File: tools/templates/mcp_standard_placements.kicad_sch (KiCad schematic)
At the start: 150 parts, among them J1 ICSP, J3 PIR BOARD, J5 MOTOR, J6 DNP, Q1 FMOS3401A?, Q11 MMBTA55?, Q2 BC847B?, Q3 MMBTA55?, Q4 MMBTA55?, Q5 MMBTA55?, Q6 MMBTA55?, Q7 BC857C?, Q8 N/P pair? (372A), Q9 DNP, U1 S-1200B45? [pins], U106 U6A / DNP, U2 SN74LVC2G14DBV?, U3 SGM8542XS, U4 PIC16F18855, U5 MX512H, U6 S-812C33AMC? / 3.3V, U7 DNP, Y1 20 MHz

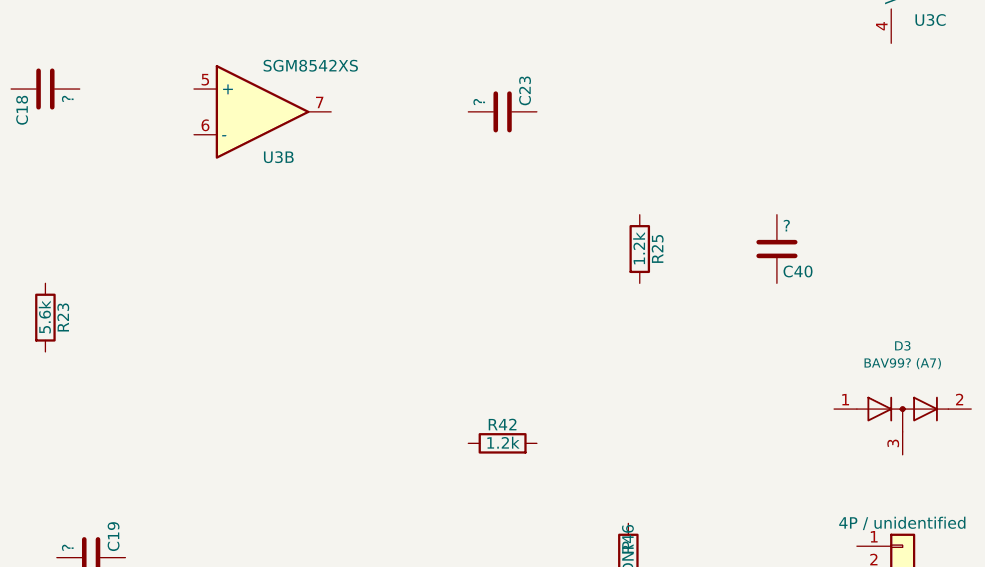
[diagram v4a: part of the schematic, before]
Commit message: Resolve R23 junction and require photo tracing before bench requests
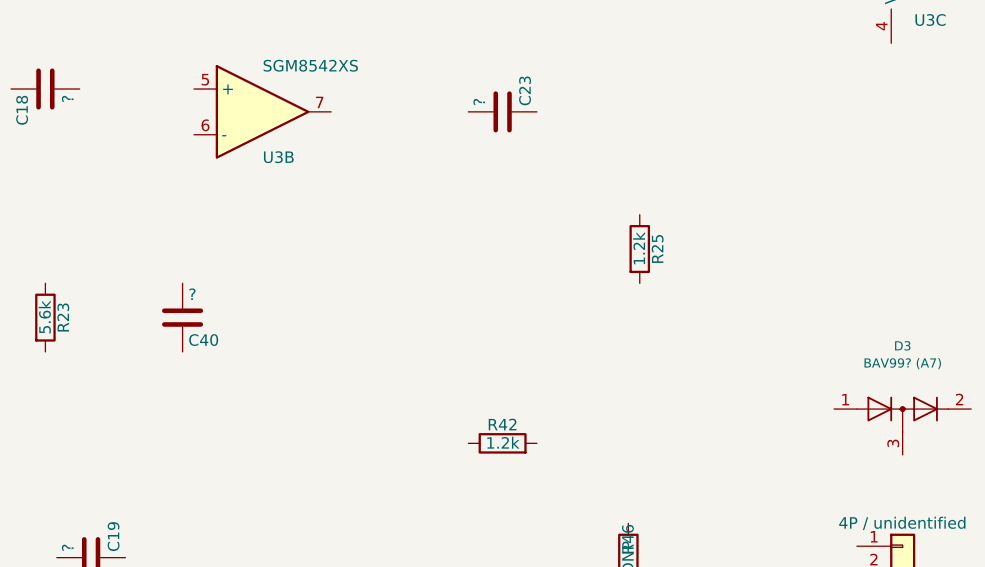
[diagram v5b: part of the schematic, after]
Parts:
- C40: MeasurementEvidence (none) -> v0.9.15: lower P/model1 joins R23 C/model2 and R42 Q/model1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; ViaEvidence v0.9.2: V083 associated with C40; earlier GND report retain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 -> v0.9.15: lower P/model1 joins R23 C/model2 and R42 Q/model1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
- R23: MeasurementEvidence v0.9.14 user: B/left/model1-U3.6 1 ohm; C/right/model2-U3.6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 -> v0.9.15: right C/model2 joins C40 lower P/model1 and R42 up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; ViaEvidence v0.9.14 user: B/left/model1-U3.6 1 ohm; C/right/model2-U3.6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 -> v0.9.15: right C/model2 joins C40 lower P/model1 and R42 up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
- R42: MeasurementEvidence (none) -> v0.9.15: upper Q/model1 joins R23 C/model2 and C40 P/model1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; ViaEvidence v0.9.8: User confirms V017-TP4. Prior V017-R42.1/R44.1 loca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 -> v0.9.15: upper Q/model1 joins R23 C/model2 and C40 P/model1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
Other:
- moved on the sheet: C40
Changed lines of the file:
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@@
 			)
 		)
-    (property "MeasurementEvidence" "v0.9.14 user: pin5-VREF/R22 D 1 ohm (batch1); pin6-R23 B/left/model1 1 ohm and C/right/model2 5.6 kohm. Pin6-R22 E/GND 400 kohm. Pin5 and pin6 remain distinct; C18 branch is retained photo evidence, not meter-confirmed." (at 381.0 200.66 0)
-      (effects (font (size 1.27 1.27)) (hide yes))
-    )
+		(property "MeasurementEvidence" "v0.9.14 user: pin5-VREF/R22 D 1 ohm (batch1); pin6-R23 B/left/model1 1 ohm and C/right/model2 5.6 kohm. Pin6-R22 E/GND 400 kohm. Pin5 and pin6 remain distinct; C18 branch is retained photo evidence, not meter-confirmed."
+			(at 381.0 200.66 0)
+			(effects
+				(font
+					(size 1.27 1.27)
+				)
+				(hide yes)
+			)
+		)
 		(pin "1"
 		)
@@
 			)
 		)
-		(property "ViaEvidence" "v0.9.14 user: B/left/model1-U3.6 1 ohm; C/right/model2-U3.6 5.6 kohm, agreeing with 562 marking. C destination remains open; earlier VREF guess rejected by 270-289 kohm to pin5. Pin6-GND 400 kohm also rejects a direct pin6-ground join."
+		(property "ViaEvidence" "v0.9.15: right C/model2 joins C40 lower P/model1 and R42 upper Q/model1 at 1 ohm each. Left B/model1 joins U3.6 (prior 1 ohm); marked 5.6k retained. C18 ends/TP6/VREF direct joins rejected by prior high readings. R42.1 remote PIC/TP4 association retained from earlier user reports."
+			(at 461.01 223.52 0)
+			(effects
+				(font
+					(size 1.27 1.27)
+				)
+				(hide yes)
+			)
+		)
+		(property "MeasurementEvidence" "v0.9.15: right C/model2 joins C40 lower P/model1 and R42 upper Q/model1 at 1 ohm each. Left B/model1 joins U3.6 (prior 1 ohm); marked 5.6k retained. C18 ends/TP6/VREF direct joins rejected by prior high readings. R42.1 remote PIC/TP4 association retained from earlier user reports."
 			(at 461.01 223.52 0)
 			(effects
 				(font
 					(size 1.27 1.27)
-				) (hide yes))
+				)
+				(hide yes)
+			)
 		)
-    (property "MeasurementEvidence" "v0.9.14 user: B/left/model1-U3.6 1 ohm; C/right/model2-U3.6 5.6 kohm, agreeing with 562 marking. C destination remains open; earlier VREF guess rejected by 270-289 kohm to pin5. Pin6-GND 400 kohm also rejects a direct pin6-ground join." (at 461.01 223.52 0)
-      (effects (font (size 1.27 1.27)) (hide yes))
-    )
 		(pin "1"
 		)
@@
 	(symbol
 		(lib_id "Device:C")
-		(at 542.29 215.9 0)
+		(at 476.25 223.52 0)
 		(unit 1)
 		(body_style 1)
@@
 		(dnp no)
 		(property "Reference" "C40"
-			(at 542.925 218.44 0)
+			(at 476.885 226.06 0)
 			(show_name no)
 			(do_not_autoplace no)
@@
 		)
 		(property "Value" "?"
-			(at 542.925 213.36 0)
+			(at 476.885 220.98000000000002 0)
 			(show_name no)
 			(do_not_autoplace no)
@@
 		)
 		(property "Footprint" "Capacitor_SMD:C_0805_2012Metric"
-			(at 543.255 212.09 0)
+			(at 477.21500000000003 219.71 0)
 			(hide yes)
 			(show_name no)
@@
 		)
 		(property "Datasheet" ""
-			(at 542.29 215.9 0)
+			(at 476.25 223.52 0)
 			(hide yes)
 			(show_name no)
@@
 		)
 		(property "Description" "Unpolarized capacitor"
-			(at 542.29 215.9 0)
+			(at 476.25 223.52 0)
 			(hide yes)
 			(show_name no)
@@
 			)
 		)
-		(property "ViaEvidence" "v0.9.2: V083 associated with C40; earlier GND report retained for photo-selected return pad2."
-			(at 542.29 215.9 0)
+		(property "ViaEvidence" "v0.9.15: lower P/model1 joins R23 C/model2 and R42 Q/model1, user 1 ohm. Remove prior C23/R25 detector-output association. Upper/model2 remains GND via user V083 report plus photo pad selection. Capacitance unmeasured."
+			(at 476.25 223.52 0)
+			(effects
+				(font
+					(size 1.27 1.27)
+				)
+				(hide yes)
+			)
+		)
+		(property "MeasurementEvidence" "v0.9.15: lower P/model1 joins R23 C/model2 and R42 Q/model1, user 1 ohm. Remove prior C23/R25 detector-output association. Upper/model2 remains GND via user V083 report plus photo pad selection. Capacitance unmeasured."
+			(at 476.25 223.52 0)
 			(effects
 				(font
@@
 			)
 		)
-		(property "ViaEvidence" "v0.9.8: User confirms V017-TP4. Prior V017-R42.1/R44.1 local junction now joins TP4 and PIC25/RB4. R42.1 explicitly user-named; R44 pad1 and C41 branch retain earlier photo selection. No numeric resistance supplied; circuit operating role remains inferred."
+		(property "ViaEvidence" "v0.9.15: upper Q/model1 joins R23 C/model2 and C40 P/model1 at 1 ohm. Prior V017/TP4/PIC25/R44.1 mapping retained. Lower/model2 to D3.S is photo-selected, supported by earlier component-level 1.2 ohm reading without named end. Marked 1.2k retained."
+			(at 511.81 237.49 0)
+			(effects
+				(font
+					(size 1.27 1.27)
+				)
+				(hide yes)
+			)
+		)
+		(property "MeasurementEvidence" "v0.9.15: upper Q/model1 joins R23 C/model2 and C40 P/model1 at 1 ohm. Prior V017/TP4/PIC25/R44.1 mapping retained. Lower/model2 to D3.S is photo-selected, supported by earlier component-level 1.2 ohm reading without named end. Marked 1.2k retained."
 			(at 511.81 237.49 0)
 			(effects
@@
 				(font
 					(size 1.27 1.27)
-				) (hide yes))
+				)
+				(hide yes)
+			)
+		)
+		(property "MeasurementEvidence" "v0.9.14 user: E/right/model1-GND 1 ohm; D/left/model2-VREF confirmed in batch1. R22 spans VREF to GND; 10 kohm agrees with 01C marking. U3 pin6 to E is 400 kohm and is not a wire."
+			(at 326.39 229.87 0)
+			(effects
+				(font
+					(size 1.27 1.27)
+				)
+				(hide yes)
+			)
 		)
-    (property "MeasurementEvidence" "v0.9.14 user: E/right/model1-GND 1 ohm; D/left/model2-VREF confirmed in batch1. R22 spans VREF to GND; 10 kohm agrees with 01C marking. U3 pin6 to E is 400 kohm and is not a wire." (at 326.39 229.87 0)
-      (effects (font (size 1.27 1.27)) (hide yes))
-    )
 		(pin "1"
 		)
@@
 			)
 		)
-    (property "MeasurementEvidence" "User confirms empty R46 footprint: upper pad/model1 joins D2.L/ANT2; lower pad/model2 joins D2.S. Remains DNP; no conducting bridge is fitted." (at 525.78 250.19 0)
-      (effects (font (size 1.27 1.27)) (hide yes))
-    )
+		(property "MeasurementEvidence" "User confirms empty R46 footprint: upper pad/model1 joins D2.L/ANT2; lower pad/model2 joins D2.S. Remains DNP; no conducting bridge is fitted."
+			(at 525.78 250.19 0)
+			(effects
+				(font
+					(size 1.27 1.27)
+				)
+				(hide yes)
+			)
+		)
 		(pin "1"
 		)
@@
 				(font
 					(size 1.27 1.27)
-				) (hide yes))
+				)
+				(hide yes)
+			)
+		)
+		(property "MeasurementEvidence" "v0.9.14 user: pin1 PIR supply previously confirmed; pin2 H-R38 K/right/model1 1 ohm and H-R38 J/left/model2 10 kohm; pin3-GND 1 ohm. Pin2-GND remains 290 kohm (batch1), distinct from ground. Q2 onward/controller route remains unverified."
+			(at 405.13 327.66 0)
+			(effects
+				(font
+					(size 1.27 1.27)
+				)
+				(hide yes)
+			)
 		)
-    (property "MeasurementEvidence" "v0.9.14 user: pin1 PIR supply previously confirmed; pin2 H-R38 K/right/model1 1 ohm and H-R38 J/left/model2 10 kohm; pin3-GND 1 ohm. Pin2-GND remains 290 kohm (batch1), distinct from ground. Q2 onward/controller route remains unverified." (at 405.13 327.66 0)
-      (effects (font (size 1.27 1.27)) (hide yes))
-    )
 		(pin "1"
 		)
@@
 			)
 		)
-    (property "MeasurementEvidence" "v0.9.14 user: K/right/model1-J3.2 1 ohm; J/left/model2-J3.2 10 kohm, agreeing with 01C marking. Q2/R39 and R33 branches remain prior hypotheses beyond this measured pair." (at 341.63 345.44 0)
-      (effects (font (size 1.27 1.27)) (hide yes))
-    )
+		(property "MeasurementEvidence" "v0.9.14 user: K/right/model1-J3.2 1 ohm; J/left/model2-J3.2 10 kohm, agreeing with 01C marking. Q2/R39 and R33 branches remain prior hypotheses beyond this measured pair."
+			(at 341.63 345.44 0)
+			(effects
+				(font
+					(size 1.27 1.27)
+				)
+				(hide yes)
+			)
+		)
 		(pin "1"
 		)
